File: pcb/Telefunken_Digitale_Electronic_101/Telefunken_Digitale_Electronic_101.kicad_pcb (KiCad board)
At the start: 2 copper layers, 100 x 52 mm, 30 parts, among them J1 Conn_01x02_Socket, J2 Conn_01x02_Socket, J3 Conn_01x02_Socket, J4 Conn_01x02_Socket, J5 Conn_01x02_Socket, J6 Conn_01x02_Socket, J7 Conn_01x02_MountingPin, J8 Conn_01x04_MountingPin, SW1 SW_Push, SW2 SW_Push, U1 TM1637_SOP20, U3 DS3231

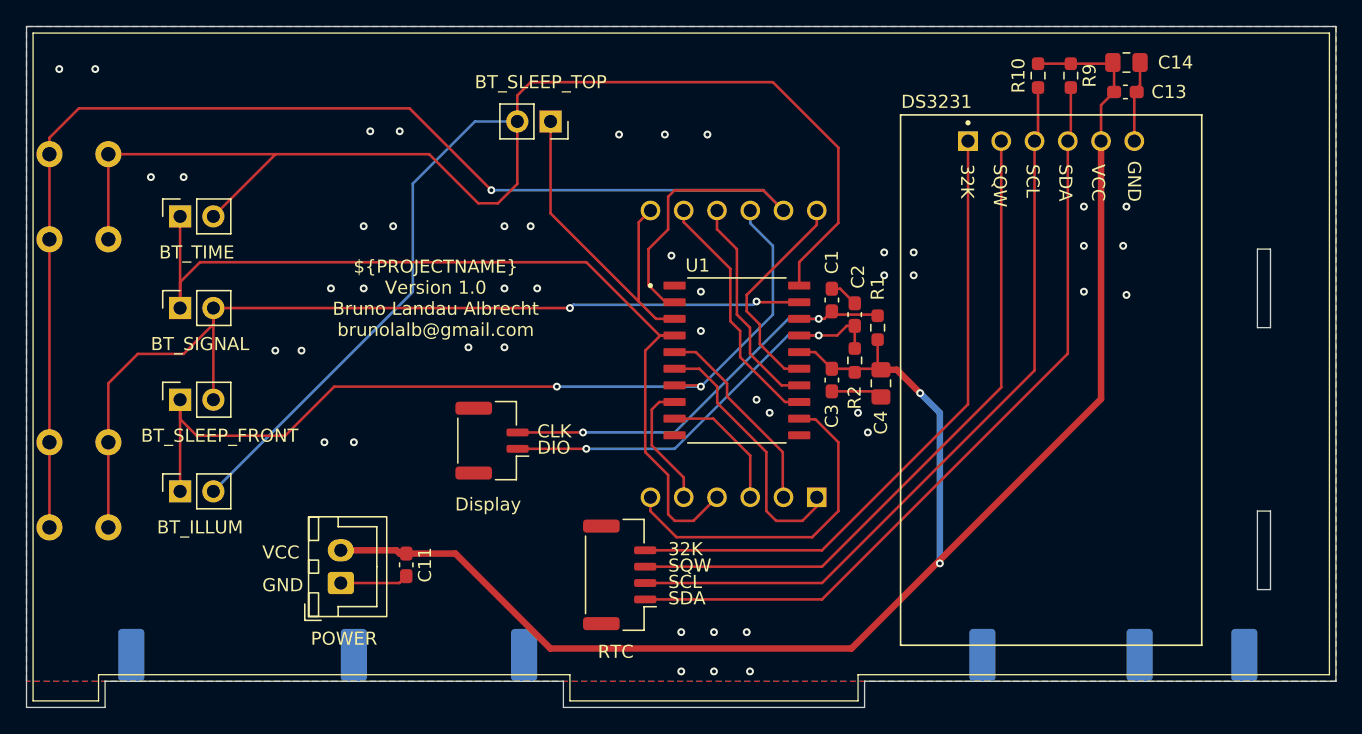
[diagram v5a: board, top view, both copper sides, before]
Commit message: SCH and PCB: reannotated everything
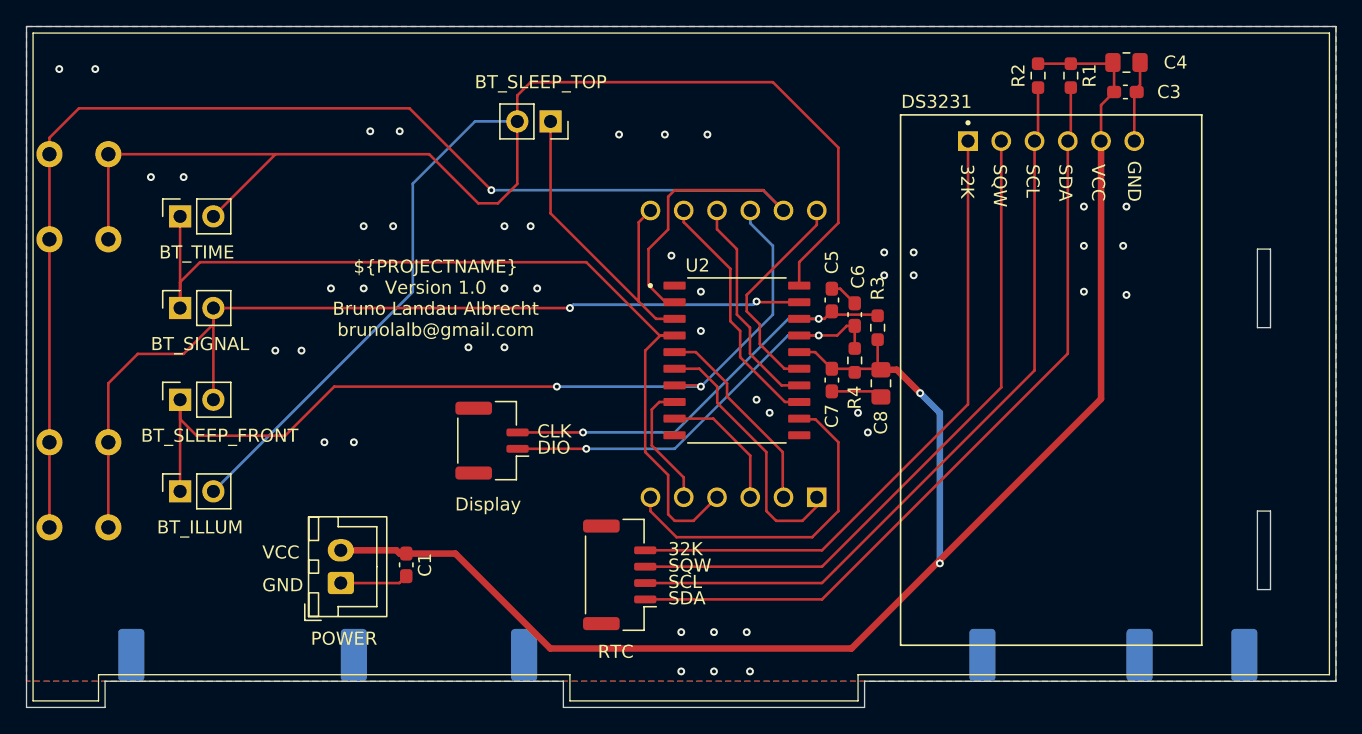
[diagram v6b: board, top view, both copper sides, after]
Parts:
- renumbered C11 to C1, C13 to C3, C14 to C4, C1 to C5, C2 to C6, C3 to C7, C4 to C8, J6 to J1, J7 to J2, J8 to J3, J1 to J4, J2 to J5, J3 to J6, J4 to J7, J5 to J8, R9 to R1, R10 to R2, R1 to R3, R2 to R4, U3 to U1, U1 to U2
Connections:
- U2 pad 10: unconnected-(U1-GRID6-Pad10) -> (no net)
- U2 pad 11: unconnected-(U1-GRID5-Pad11) -> (no net)
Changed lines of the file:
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@@
 		(descr "Through hole straight socket strip, 1x02, 2.54mm pitch, single row (from Kicad 4.0.7), script generated")
 		(tags "Through hole socket strip THT 1x02 2.54mm single row")
-		(property "Reference" "J1"
+		(property "Reference" "J4"
 			(at 0 -2.77 90)
 			(layer "F.SilkS")
@@
 		(descr "Capacitor SMD 0603 (1608 Metric), square (rectangular) end terminal, IPC-7351 nominal with elongated pad for handsoldering. (Body size source: IPC-SM-782 page 76, https://www.pcb-3d.com/wordpress/wp-content/uploads/ipc-sm-782a_amendment_1_and_2.pdf)")
 		(tags "capacitor handsolder")
-		(property "Reference" "C13"
+		(property "Reference" "C3"
 			(at 3.33 0 0)
 			(layer "F.SilkS")
@@
 		(descr "Capacitor SMD 0603 (1608 Metric), square (rectangular) end terminal, IPC-7351 nominal with elongated pad for handsoldering. (Body size source: IPC-SM-782 page 76, https://www.pcb-3d.com/wordpress/wp-content/uploads/ipc-sm-782a_amendment_1_and_2.pdf)")
 		(tags "capacitor handsolder")
-		(property "Reference" "C3"
+		(property "Reference" "C7"
 			(at 2.75 0 90)
 			(layer "F.SilkS")
@@
 		(descr "Capacitor SMD 0603 (1608 Metric), square (rectangular) end terminal, IPC-7351 nominal with elongated pad for handsoldering. (Body size source: IPC-SM-782 page 76, https://www.pcb-3d.com/wordpress/wp-content/uploads/ipc-sm-782a_amendment_1_and_2.pdf)")
 		(tags "capacitor handsolder")
-		(property "Reference" "C2"
+		(property "Reference" "C6"
 			(at 2.8875 0.25 90)
 			(layer "F.SilkS")
@@
 		(descr "Resistor SMD 0603 (1608 Metric), square (rectangular) end terminal, IPC-7351 nominal with elongated pad for handsoldering. (Body size source: IPC-SM-782 page 72, https://www.pcb-3d.com/wordpress/wp-content/uploads/ipc-sm-782a_amendment_1_and_2.pdf)")
 		(tags "resistor handsolder")
-		(property "Reference" "R10"
+		(property "Reference" "R2"
 			(at 0 1.5 90)
 			(layer "F.SilkS")
@@
 		(layer "F.Cu")
 		(at 154.25 75.5)
-		(property "Reference" "U1"
+		(property "Reference" "U2"
 			(at -3 -7.25 0)
 			(layer "F.SilkS")
@@
 			(layers "F.Cu" "F.Mask" "F.Paste")
 			(roundrect_rratio 0.125)
-			(net "unconnected-(U1-GRID6-Pad10)")
 			(pinfunction "GRID6_10")
 			(pintype "output+no_connect")
@@
 			(layers "F.Cu" "F.Mask" "F.Paste")
 			(roundrect_rratio 0.125)
-			(net "unconnected-(U1-GRID5-Pad11)")
 			(pinfunction "GRID5_11")
 			(pintype "output+no_connect")
@@
 		(descr "Resistor SMD 0603 (1608 Metric), square (rectangular) end terminal, IPC-7351 nominal with elongated pad for handsoldering. (Body size source: IPC-SM-782 page 72, https://www.pcb-3d.com/wordpress/wp-content/uploads/ipc-sm-782a_amendment_1_and_2.pdf)")
 		(tags "resistor handsolder")
-		(property "Reference" "R9"
+		(property "Reference" "R1"
 			(at 0 -1.43 90)
 			(layer "F.SilkS")
@@
 		(descr "Capacitor SMD 0603 (1608 Metric), square (rectangular) end terminal, IPC-7351 nominal with elongated pad for handsoldering. (Body size source: IPC-SM-782 page 76, https://www.pcb-3d.com/wordpress/wp-content/uploads/ipc-sm-782a_amendment_1_and_2.pdf)")
 		(tags "capacitor handsolder")
-		(property "Reference" "C11"
+		(property "Reference" "C1"
 			(at 0 -1.43 90)
 			(layer "F.SilkS")
@@
 		(descr "Through hole straight socket strip, 1x02, 2.54mm pitch, single row (from Kicad 4.0.7), script generated")
 		(tags "Through hole socket strip THT 1x02 2.54mm single row")
-		(property "Reference" "J3"
+		(property "Reference" "J6"
 			(at 0 -2.77 90)
 			(layer "F.SilkS")
@@
 		(descr "Resistor SMD 0603 (1608 Metric), square (rectangular) end terminal, IPC-7351 nominal with elongated pad for handsoldering. (Body size source: IPC-SM-782 page 72, https://www.pcb-3d.com/wordpress/wp-content/uploads/ipc-sm-782a_amendment_1_and_2.pdf)")
 		(tags "resistor handsolder")
-		(property "Reference" "R1"
+		(property "Reference" "R3"
 			(at 3 0 90)
 			(layer "F.SilkS")
@@
 		(descr "Capacitor SMD 0603 (1608 Metric), square (rectangular) end terminal, IPC-7351 nominal with elongated pad for handsoldering. (Body size source: IPC-SM-782 page 76, https://www.pcb-3d.com/wordpress/wp-content/uploads/ipc-sm-782a_amendment_1_and_2.pdf)")
 		(tags "capacitor handsolder")
-		(property "Reference" "C1"
+		(property "Reference" "C5"
 			(at 2.8875 0 90)
 			(layer "F.SilkS")
@@
 		(descr "JST GH series connector, BM02B-GHS-TBT (http://www.jst-mfg.com/product/pdf/eng/eGH.pdf)")
 		(tags "connector JST GH vertical")
-		(property "Reference" "J7"
+		(property "Reference" "J2"
 			(at 0 -4 90)
 			(layer "F.SilkS")
@@
 		(descr "JST GH series connector, BM04B-GHS-TBT (http://www.jst-mfg.com/product/pdf/eng/eGH.pdf)")
 		(tags "connector JST GH vertical")
-		(property "Reference" "J8"
+		(property "Reference" "J3"
 			(at 0 -4 90)
 			(layer "F.SilkS")
@@
 		(descr "Resistor SMD 0603 (1608 Metric), square (rectangular) end terminal, IPC-7351 nominal with elongated pad for handsoldering. (Body size source: IPC-SM-782 page 72, https://www.pcb-3d.com/wordpress/wp-content/uploads/ipc-sm-782a_amendment_1_and_2.pdf)")
 		(tags "resistor handsolder")
-		(property "Reference" "R2"
+		(property "Reference" "R4"
 			(at -2.8375 -0.01 90)
 			(layer "F.SilkS")
@@
 		(descr "JST XH series connector, B2B-XH-A (http://www.jst-mfg.com/product/pdf/eng/eXH.pdf)")
 		(tags "connector JST XH vertical")
-		(property "Reference" "J6"
+		(property "Reference" "J1"
 			(at 1.25 -3.55 90)
 			(layer "F.SilkS")
@@
 		(descr "Through hole straight socket strip, 1x02, 2.54mm pitch, single row (from Kicad 4.0.7), script generated")
 		(tags "Through hole socket strip THT 1x02 2.54mm single row")
-		(property "Reference" "J4"
+		(property "Reference" "J7"
 			(at 0 -2.77 90)
 			(layer "F.SilkS")
@@
 		(descr "Through hole straight socket strip, 1x02, 2.54mm pitch, single row (from Kicad 4.0.7), script generated")
 		(tags "Through hole socket strip THT 1x02 2.54mm single row")
-		(property "Reference" "J2"
+		(property "Reference" "J5"
 			(at 0 -2.77 90)
 			(layer "F.SilkS")
@@
 		(descr "Capacitor SMD 0805 (2012 Metric), square (rectangular) end terminal, IPC-7351 nominal with elongated pad for handsoldering. (Body size source: IPC-SM-782 page 76, https://www.pcb-3d.com/wordpress/wp-content/uploads/ipc-sm-782a_amendment_1_and_2.pdf, https://docs.google.com/spreadsheets/d/1BsfQQcO9C6DZCsRaXUlFlo91Tg2WpOkGARC1WS5S8t0/edit?usp=sharing)")
 		(tags "capacitor handsolder")
-		(property "Reference" "C4"
+		(property "Reference" "C8"
 			(at 3 0 90)
 			(layer "F.SilkS")
@@
 		(descr "Through hole straight socket strip, 1x02, 2.54mm pitch, single row (from Kicad 4.0.7), script generated")
 		(tags "Through hole socket strip THT 1x02 2.54mm single row")
-		(property "Reference" "J5"
+		(property "Reference" "J8"
 			(at 0 -2.77 90)
 			(layer "F.SilkS")
@@
 		(layer "F.Cu")
 		(at 178.25 58.75 -90)
-		(property "Reference" "U3"
+		(property "Reference" "U1"
 			(at 3.175 -12.135 90)
 			(layer "F.SilkS")
@@
 		(descr "Capacitor SMD 0805 (2012 Metric), square (rectangular) end terminal, IPC-7351 nominal with elongated pad for handsoldering. (Body size source: IPC-SM-782 page 76, https://www.pcb-3d.com/wordpress/wp-content/uploads/ipc-sm-782a_amendment_1_and_2.pdf, https://docs.google.com/spreadsheets/d/1BsfQQcO9C6DZCsRaXUlFlo91Tg2WpOkGARC1WS5S8t0/edit?usp=sharing)")
 		(tags "capacitor handsolder")
-		(property "Reference" "C14"
+		(property "Reference" "C4"
 			(at 3.75 0 0)
 			(layer "F.SilkS")

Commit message: adjusted connectors footprints, added footprint to input polarized capacitor, rtc and display polarized capacitors converted to non polarized
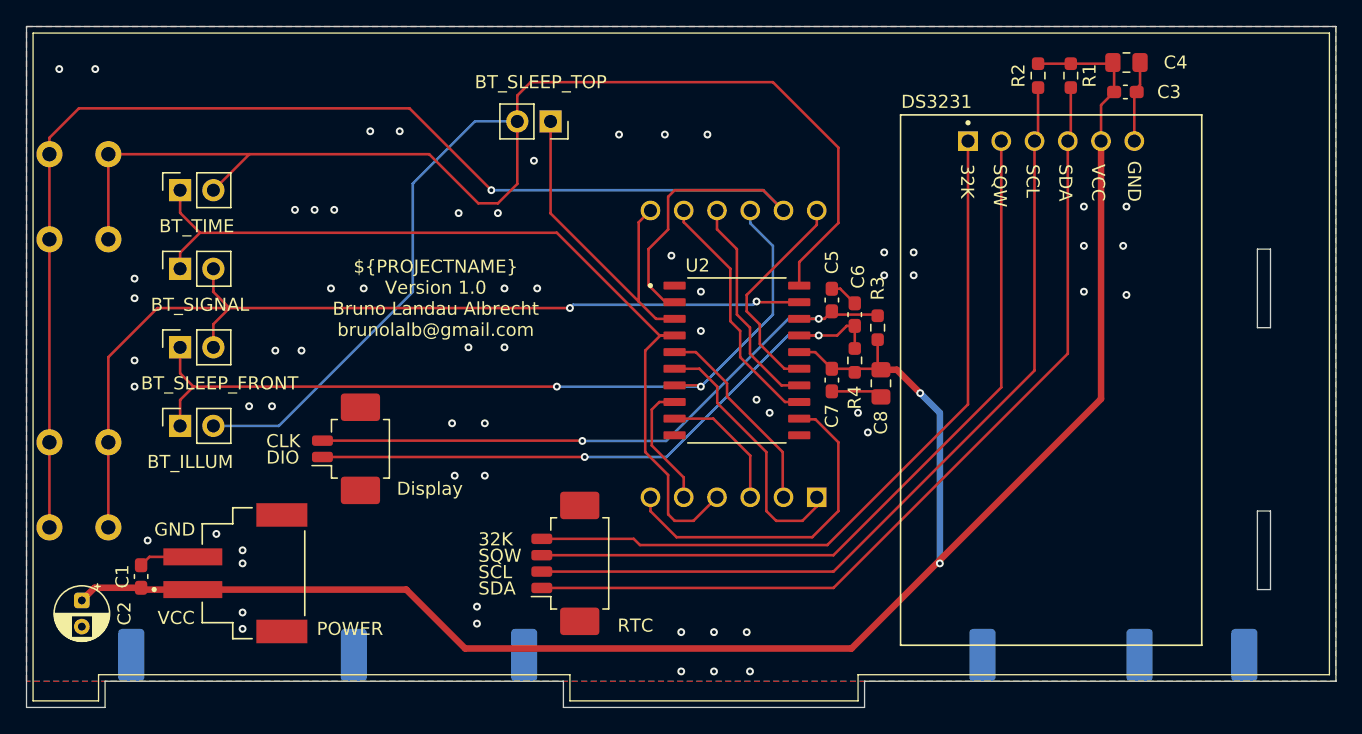
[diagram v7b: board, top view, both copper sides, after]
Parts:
- added C2: 10u, Capacitor_THT:CP_Radial_D4.0mm_P2.00mm, F.Cu at (104.2, 93.8)
- J1: value Conn_01x02_Socket -> Conn_01x02_MountingPin; footprint Connector_JST:JST_XH_B2B-XH-A_1x02_P2.50mm_Vertical -> RadioWecker:JST_S2B-XH-SM4-TB
- J2: footprint Connector_JST:JST_GH_BM02B-GHS-TBT_1x02-1MP_P1.25mm_Vertical -> Connector_Molex:Molex_PicoBlade_53261-0271_1x02-1MP_P1.25mm_Horizontal
- J3: footprint Connector_JST:JST_GH_BM04B-GHS-TBT_1x04-1MP_P1.25mm_Vertical -> Connector_Molex:Molex_PicoBlade_53261-0471_1x04-1MP_P1.25mm_Horizontal
- moved C1 20.3 mm to (108.8, 92.0), turned to 90 degrees
- moved J2 10.6 mm to (125.0, 82.2)
- moved J7 5.00 mm to (111.7, 80.5)
- moved J1 4.56 mm to (119.5, 91.8)
- moved J6 4.00 mm to (111.7, 74.5)
- moved J3 3.66 mm to (141.8, 91.0)
- moved J5 3.00 mm to (111.7, 68.5)
- moved J4 2.00 mm to (111.7, 62.5)
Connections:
- J1 pad 1: GND -> VCC
- J1 pad 2: VCC -> GND
- U2 pad 10: (no net) -> unconnected-(U2-GRID6-Pad10)
- U2 pad 11: (no net) -> unconnected-(U2-GRID5-Pad11)
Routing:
- net VCC: track 127.5 -> 146.5 mm
- net /Display/CLK: track 33.0 -> 48.1 mm
- net /Display/DIO: track 32.9 -> 48.0 mm
- net /Interface/RTC_32K: track 49.4 -> 57.3 mm
- net /Interface/RTC_SDA: track 60.5 -> 68.0 mm
- net /Interface/RTC_SQW: track 51.7 -> 59.2 mm
- net /Interface/RTC_SCL: track 58.2 -> 65.7 mm
- net /Buttons/K2: track 131.9 -> 127.0 mm
- net /Buttons/GRID4: track 68.8 -> 64.1 mm
- net /Buttons/GRID3: track 70.3 -> 67.4 mm
- net GND: track 17.5 -> 16.5 mm, vias 46 -> 62
